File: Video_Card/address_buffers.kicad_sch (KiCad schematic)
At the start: 3 parts, among them U2 74FCT162244, U3 74FCT162244, U4 SN74AHCT1G32DBV

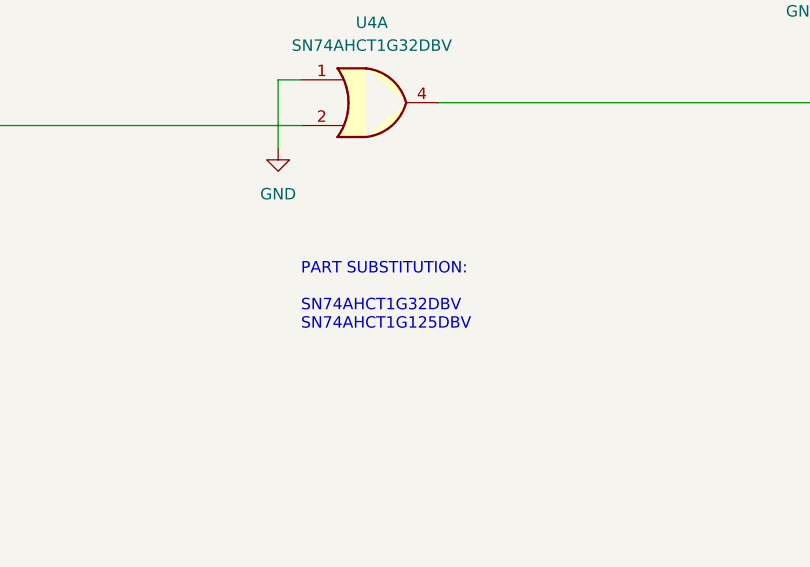
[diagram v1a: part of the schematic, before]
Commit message: Work to date:
* added RAMDAC sheet
* tweaks to promulator circuit to disconnect MCLR, and add future reset output
* tweaks to FPGA host interface, add pin numbers and rearrange reset input to allow reset either from the system or from the promulator following configuration
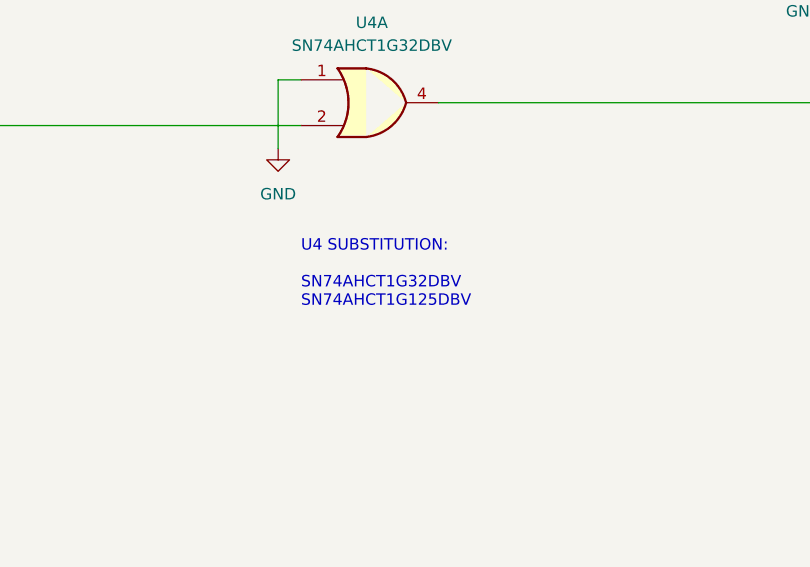
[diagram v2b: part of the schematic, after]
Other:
- note added: "U4 SUBSTITUTION: SN74AHCT1G32DBV SN74AHCT1G125DBV"
- note removed: "PART SUBSTITUTION: SN74AHCT1G32DBV SN74AHCT1G125DBV"
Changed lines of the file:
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@@
 		)
 	)
-	(text "PART SUBSTITUTION:\n\nSN74AHCT1G32DBV\nSN74AHCT1G125DBV"
+	(text "U4 SUBSTITUTION:\n\nSN74AHCT1G32DBV\nSN74AHCT1G125DBV"
 		(exclude_from_sim no)
-		(at 134.62 160.02 0)
+		(at 134.62 157.48 0)
 		(effects
 			(font

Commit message: Progress as of returning from travel
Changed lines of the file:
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@@
 	(wire
 		(pts
+			(xy 134.62 139.7) (xy 48.26 139.7)
+		)
+		(stroke
+			(width 0)
+			(type default)
+		)
+	)
+	(wire
+		(pts
 			(xy 101.6 86.36) (xy 111.76 86.36)
 		)
@@
 	(wire
 		(pts
-			(xy 132.08 139.7) (xy 132.08 147.32)
-		)
-		(stroke
-			(width 0)
-			(type default)
-		)
-	)
-	(wire
-		(pts
 			(xy 73.66 121.92) (xy 76.2 121.92)
 		)
@@
 	(wire
 		(pts
-			(xy 134.62 139.7) (xy 132.08 139.7)
-		)
-		(stroke
-			(width 0)
-			(type default)
-		)
-	)
-	(wire
-		(pts
 			(xy 180.34 86.36) (xy 193.04 86.36)
 		)
@@
 	(wire
 		(pts
+			(xy 129.54 144.78) (xy 129.54 149.86)
+		)
+		(stroke
+			(width 0)
+			(type default)
+		)
+	)
+	(wire
+		(pts
 			(xy 218.44 38.1) (xy 238.76 38.1)
 		)
@@
 	(wire
 		(pts
-			(xy 48.26 144.78) (xy 134.62 144.78)
-		)
-		(stroke
-			(width 0)
-			(type default)
-		)
-	)
-	(wire
-		(pts
 			(xy 63.5 40.64) (xy 76.2 40.64)
 		)
@@
 	(wire
 		(pts
+			(xy 134.62 144.78) (xy 129.54 144.78)
+		)
+		(stroke
+			(width 0)
+			(type default)
+		)
+	)
+	(wire
+		(pts
 			(xy 63.5 38.1) (xy 76.2 38.1)
 		)
@@
 	(label "A17"
 		(at 226.06 114.3 180)
+		(fields_autoplaced yes)
 		(effects
 			(font
@@
 	(label "SA4"
 		(at 66.04 91.44 0)
+		(fields_autoplaced yes)
 		(effects
 			(font
@@
 	(label "A19"
 		(at 226.06 109.22 180)
+		(fields_autoplaced yes)
 		(effects
 			(font
@@
 	(label "SA2"
 		(at 66.04 111.76 0)
+		(fields_autoplaced yes)
 		(effects
 			(font
@@
 	(label "A8"
 		(at 109.22 66.04 180)
+		(fields_autoplaced yes)
 		(effects
 			(font
@@
 	(label "SA6"
 		(at 66.04 86.36 0)
+		(fields_autoplaced yes)
 		(effects
 			(font
@@
 	(label "SA22"
 		(at 182.88 86.36 0)
+		(fields_autoplaced yes)
 		(effects
 			(font
@@
 	(label "A1"
 		(at 109.22 114.3 180)
+		(fields_autoplaced yes)
 		(effects
 			(font
@@
 	(label "A21"
 		(at 226.06 88.9 180)
+		(fields_autoplaced yes)
 		(effects
 			(font
@@
 	(label "SA9"
 		(at 66.04 63.5 0)
+		(fields_autoplaced yes)
 		(effects
 			(font
@@
 	(label "A14"
 		(at 109.22 35.56 180)
+		(fields_autoplaced yes)
 		(effects
 			(font
@@
 	(label "SA13"
 		(at 66.04 38.1 0)
+		(fields_autoplaced yes)
 		(effects
 			(font
@@
 	(label "A18"
 		(at 226.06 111.76 180)
+		(fields_autoplaced yes)
 		(effects
 			(font
@@
 	(label "SA14"
 		(at 66.04 35.56 0)
+		(fields_autoplaced yes)
 		(effects
 			(font
@@
 	(label "SA5"
 		(at 66.04 88.9 0)
+		(fields_autoplaced yes)
 		(effects
 			(font
@@
 	(label "SA16"
 		(at 182.88 116.84 0)
+		(fields_autoplaced yes)
 		(effects
 			(font
@@
 	(label "A2"
 		(at 109.22 111.76 180)
+		(fields_autoplaced yes)
 		(effects
 			(font
@@
 	(label "SA7"
 		(at 66.04 83.82 0)
+		(fields_autoplaced yes)
 		(effects
 			(font
@@
 	(label "A12"
 		(at 109.22 40.64 180)
+		(fields_autoplaced yes)
 		(effects
 			(font
@@
 	(label "A4"
 		(at 109.22 91.44 180)
+		(fields_autoplaced yes)
 		(effects
 			(font
@@
 	(label "SA1"
 		(at 66.04 114.3 0)
+		(fields_autoplaced yes)
 		(effects
 			(font
@@
 	(label "A9"
 		(at 109.22 63.5 180)
+		(fields_autoplaced yes)
 		(effects
 			(font
@@
 	(label "A13"
 		(at 109.22 38.1 180)
+		(fields_autoplaced yes)
 		(effects
 			(font
@@
 	(label "SA19"
 		(at 182.88 109.22 0)
+		(fields_autoplaced yes)
 		(effects
 			(font
@@
 	(label "SA12"
 		(at 66.04 40.64 0)
+		(fields_autoplaced yes)
 		(effects
 			(font
@@
 	(label "A7"
 		(at 109.22 83.82 180)
+		(fields_autoplaced yes)
 		(effects
 			(font
@@
 	(label "SA17"
 		(at 182.88 114.3 0)
+		(fields_autoplaced yes)
 		(effects
 			(font
@@
 	(label "A6"
 		(at 109.22 86.36 180)
+		(fields_autoplaced yes)
 		(effects
 			(font
@@
 	(label "A11"
 		(at 109.22 58.42 180)
+		(fields_autoplaced yes)
 		(effects
 			(font
@@
 	(label "SA21"
 		(at 182.88 88.9 0)
+		(fields_autoplaced yes)
 		(effects
 			(font
@@
 	(label "A16"
 		(at 226.06 116.84 180)
+		(fields_autoplaced yes)
 		(effects
 			(font
@@
 	(label "SA3"
 		(at 66.04 109.22 0)
+		(fields_autoplaced yes)
 		(effects
 			(font
@@
 	(label "A3"
 		(at 109.22 109.22 180)
+		(fields_autoplaced yes)
 		(effects
 			(font
@@
 	(label "A20"
 		(at 226.06 91.44 180)
+		(fields_autoplaced yes)
 		(effects
 			(font
@@
 	(label "SA8"
 		(at 66.04 66.04 0)
+		(fields_autoplaced yes)
 		(effects
 			(font
@@
 	(label "SA15"
 		(at 66.04 33.02 0)
+		(fields_autoplaced yes)
 		(effects
 			(font
@@
 	(label "A22"
 		(at 226.06 86.36 180)
+		(fields_autoplaced yes)
 		(effects
 			(font
@@
 	(label "SA23"
 		(at 182.88 83.82 0)
+		(fields_autoplaced yes)
 		(effects
 			(font
@@
 	(label "SA11"
 		(at 66.04 58.42 0)
+		(fields_autoplaced yes)
 		(effects
 			(font
@@
 	(label "A15"
 		(at 109.22 33.02 180)
+		(fields_autoplaced yes)
 		(effects
 			(font
@@
 	(label "A10"
 		(at 109.22 60.96 180)
+		(fields_autoplaced yes)
 		(effects
 			(font
@@
 	(label "SA20"
 		(at 182.88 91.44 0)
+		(fields_autoplaced yes)
 		(effects
 			(font
@@
 	(label "A5"
 		(at 109.22 88.9 180)
+		(fields_autoplaced yes)
 		(effects
 			(font
@@
 	(label "SA10"
 		(at 66.04 60.96 0)
+		(fields_autoplaced yes)
 		(effects
 			(font
@@
 	(label "A23"
 		(at 226.06 83.82 180)
+		(fields_autoplaced yes)
 		(effects
 			(font
@@
 	(label "SA18"
 		(at 182.88 111.76 0)
+		(fields_autoplaced yes)
 		(effects
 			(font
@@
 	(global_label "SYSCLK`"
 		(shape input)
-		(at 48.26 144.78 180)
+		(at 48.26 139.7 180)
 		(fields_autoplaced yes)
 		(effects
@@
 		)
 		(property "Intersheetrefs" "${INTERSHEET_REFS}"
-			(at 37.7153 144.78 0)
+			(at 37.7153 139.7 0)
 			(effects
 				(font
@@
 	(symbol
 		(lib_id "power:GND")
-		(at 132.08 147.32 0)
+		(at 129.54 149.86 0)
 		(unit 1)
 		(exclude_from_sim no)
@@
 		(fields_autoplaced yes)
 		(property "Reference" "#PWR06"
-			(at 132.08 153.67 0)
+			(at 129.54 156.21 0)
 			(effects
 				(font
@@
 		)
 		(property "Value" "GND"
-			(at 132.08 152.4 0)
+			(at 129.54 154.94 0)
 			(effects
 				(font
@@
 		)
 		(property "Footprint" ""
-			(at 132.08 147.32 0)
+			(at 129.54 149.86 0)
 			(effects
 				(font
@@
 		)
 		(property "Datasheet" ""
-			(at 132.08 147.32 0)
+			(at 129.54 149.86 0)
 			(effects
 				(font
@@
 		)
 		(property "Description" "Power symbol creates a global label with name \"GND\" , ground"
-			(at 132.08 147.32 0)
+			(at 129.54 149.86 0)
 			(effects
 				(font
@@
 		(lib_id "COMET_symbols:74x1G32")
 		(at 142.24 142.24 0)
+		(mirror x)
 		(unit 1)
 		(exclude_from_sim no)
@@
 		(on_board yes)
 		(dnp no)
-		(fields_autoplaced yes)
 		(property "Reference" "U4"
-			(at 142.4938 133.35 0)
+			(at 142.4938 151.13 0)
 			(effects
 				(font
@@
 		)
 		(property "Value" "SN74AHCT1G32DBV"
-			(at 142.4938 135.89 0)
+			(at 142.4938 148.59 0)
 			(effects
 				(font

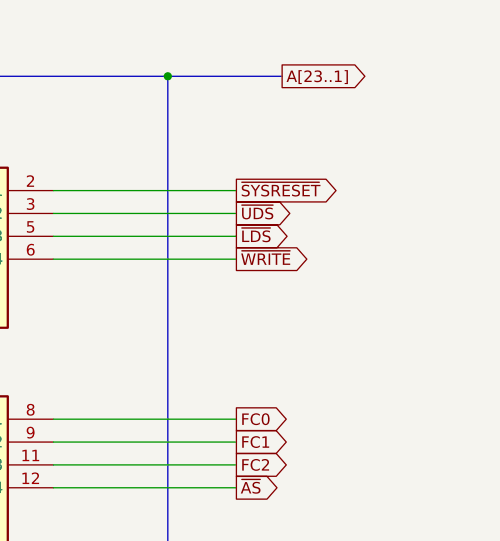
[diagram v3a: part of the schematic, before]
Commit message: Work to date
So much to list ....

* Changed expansion ROM to 16 bit wide to remove some components
* Tried moving peripherals over to an 8 bit dedicated bus, but will have to revert this to reduce component count
* Fleshed out keyboard and I2C controller circuits
* Tried to fit in a font RAM, but I am 50/50 whether this will stick

And a lot more I am sure.
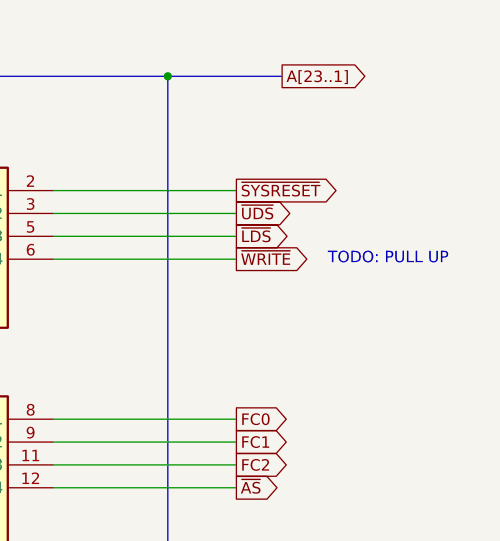
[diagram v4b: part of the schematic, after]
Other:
- note added: "TODO: PULL UP"
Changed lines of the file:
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@@
+		)
+	)
+	(text "TODO: PULL UP"
+		(exclude_from_sim no)
+		(at 248.92 40.64 0)
+		(effects
+			(font
+				(size 1.27 1.27)
+			)
+			(justify left)
 		)
 	)
@@
 	(label "A17"
 		(at 226.06 114.3 180)
-		(fields_autoplaced yes)
 		(effects
 			(font
@@
 	(label "SA4"
 		(at 66.04 91.44 0)
-		(fields_autoplaced yes)
 		(effects
 			(font
@@
 	(label "A19"
 		(at 226.06 109.22 180)
-		(fields_autoplaced yes)
 		(effects
 			(font
@@
 	(label "SA2"
 		(at 66.04 111.76 0)
-		(fields_autoplaced yes)
 		(effects
 			(font
@@
 	(label "A8"
 		(at 109.22 66.04 180)
-		(fields_autoplaced yes)
 		(effects
 			(font
@@
 	(label "SA6"
 		(at 66.04 86.36 0)
-		(fields_autoplaced yes)
 		(effects
 			(font
@@
 	(label "SA22"
 		(at 182.88 86.36 0)
-		(fields_autoplaced yes)
 		(effects
 			(font
@@
 	(label "A1"
 		(at 109.22 114.3 180)
-		(fields_autoplaced yes)
 		(effects
 			(font
@@
 	(label "A21"
 		(at 226.06 88.9 180)
-		(fields_autoplaced yes)
 		(effects
 			(font
@@
 	(label "SA9"
 		(at 66.04 63.5 0)
-		(fields_autoplaced yes)
 		(effects
 			(font
@@
 	(label "A14"
 		(at 109.22 35.56 180)
-		(fields_autoplaced yes)
 		(effects
 			(font
@@
 	(label "SA13"
 		(at 66.04 38.1 0)
-		(fields_autoplaced yes)
 		(effects
 			(font
@@
 	(label "A18"
 		(at 226.06 111.76 180)
-		(fields_autoplaced yes)
 		(effects
 			(font
@@
 	(label "SA14"
 		(at 66.04 35.56 0)
-		(fields_autoplaced yes)
 		(effects
 			(font
@@
 	(label "SA5"
 		(at 66.04 88.9 0)
-		(fields_autoplaced yes)
 		(effects
 			(font
@@
 	(label "SA16"
 		(at 182.88 116.84 0)
-		(fields_autoplaced yes)
 		(effects
 			(font
@@
 	(label "A2"
 		(at 109.22 111.76 180)
-		(fields_autoplaced yes)
 		(effects
 			(font
@@
 	(label "SA7"
 		(at 66.04 83.82 0)
-		(fields_autoplaced yes)
 		(effects
 			(font
@@
 	(label "A12"
 		(at 109.22 40.64 180)
-		(fields_autoplaced yes)
 		(effects
 			(font
@@
 	(label "A4"
 		(at 109.22 91.44 180)
-		(fields_autoplaced yes)
 		(effects
 			(font
@@
 	(label "SA1"
 		(at 66.04 114.3 0)
-		(fields_autoplaced yes)
 		(effects
 			(font
@@
 	(label "A9"
 		(at 109.22 63.5 180)
-		(fields_autoplaced yes)
 		(effects
 			(font
@@
 	(label "A13"
 		(at 109.22 38.1 180)
-		(fields_autoplaced yes)
 		(effects
 			(font
@@
 	(label "SA19"
 		(at 182.88 109.22 0)
-		(fields_autoplaced yes)
 		(effects
 			(font
@@
 	(label "SA12"
 		(at 66.04 40.64 0)
-		(fields_autoplaced yes)
 		(effects
 			(font
@@
 	(label "A7"
 		(at 109.22 83.82 180)
-		(fields_autoplaced yes)
 		(effects
 			(font
@@
 	(label "SA17"
 		(at 182.88 114.3 0)
-		(fields_autoplaced yes)
 		(effects
 			(font
@@
 	(label "A6"
 		(at 109.22 86.36 180)
-		(fields_autoplaced yes)
 		(effects
 			(font
@@
 	(label "A11"
 		(at 109.22 58.42 180)
-		(fields_autoplaced yes)
 		(effects
 			(font
@@
 	(label "SA21"
 		(at 182.88 88.9 0)
-		(fields_autoplaced yes)
 		(effects
 			(font
@@
 	(label "A16"
 		(at 226.06 116.84 180)
-		(fields_autoplaced yes)
 		(effects
 			(font
@@
 	(label "SA3"
 		(at 66.04 109.22 0)
-		(fields_autoplaced yes)
 		(effects
 			(font
@@
 	(label "A3"
 		(at 109.22 109.22 180)
-		(fields_autoplaced yes)
 		(effects
 			(font
@@
 	(label "A20"
 		(at 226.06 91.44 180)
-		(fields_autoplaced yes)
 		(effects
 			(font
@@
 	(label "SA8"
 		(at 66.04 66.04 0)
-		(fields_autoplaced yes)
 		(effects
 			(font
@@
 	(label "SA15"
 		(at 66.04 33.02 0)
-		(fields_autoplaced yes)
 		(effects
 			(font
@@
 	(label "A22"
 		(at 226.06 86.36 180)
-		(fields_autoplaced yes)
 		(effects
 			(font
@@
 	(label "SA23"
 		(at 182.88 83.82 0)
-		(fields_autoplaced yes)
 		(effects
 			(font
@@
 	(label "SA11"
 		(at 66.04 58.42 0)
-		(fields_autoplaced yes)
 		(effects
 			(font
@@
 	(label "A15"
 		(at 109.22 33.02 180)
-		(fields_autoplaced yes)
 		(effects
 			(font
@@
 	(label "A10"
 		(at 109.22 60.96 180)
-		(fields_autoplaced yes)
 		(effects
 			(font
@@
 	(label "SA20"
 		(at 182.88 91.44 0)
-		(fields_autoplaced yes)
 		(effects
 			(font
@@
 	(label "A5"
 		(at 109.22 88.9 180)
-		(fields_autoplaced yes)
 		(effects
 			(font
@@
 	(label "SA10"
 		(at 66.04 60.96 0)
-		(fields_autoplaced yes)
 		(effects
 			(font
@@
 	(label "A23"
 		(at 226.06 83.82 180)
-		(fields_autoplaced yes)
 		(effects
 			(font
@@
 	(label "SA18"
 		(at 182.88 111.76 0)
-		(fields_autoplaced yes)
-		(effects
-			(font
+		(effects
+			(font

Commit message: Final work for rev 1
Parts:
- removed unit 5 of U2
- removed unit 5 of U3
- removed U4: SN74AHCT1G32DBV, COMET_footprints:Package_SOT23-5, symbol COMET_symbols:74x1G32
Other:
- note removed: "TODO: PULL UP"
- note removed: "U4 SUBSTITUTION: SN74AHCT1G32DBV SN74AHCT1G125DBV"
- moved on the sheet: U2A, U2B, U2C, U2D, U3A, U3B, U3C, U3D
